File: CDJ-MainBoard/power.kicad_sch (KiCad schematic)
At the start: 46 parts, among them J15 USB_C_Receptacle_USB2.0_16P, SW3 SW_MAIN_POWER, U1 Compute_Module_5_Functional, U10 AP2112K-3.3 DIGITAL PSU LDO, U11 AP2112K-3.3 ANALOG AUDIO LDO, U12 CH224K, U13 SY8368AQQC

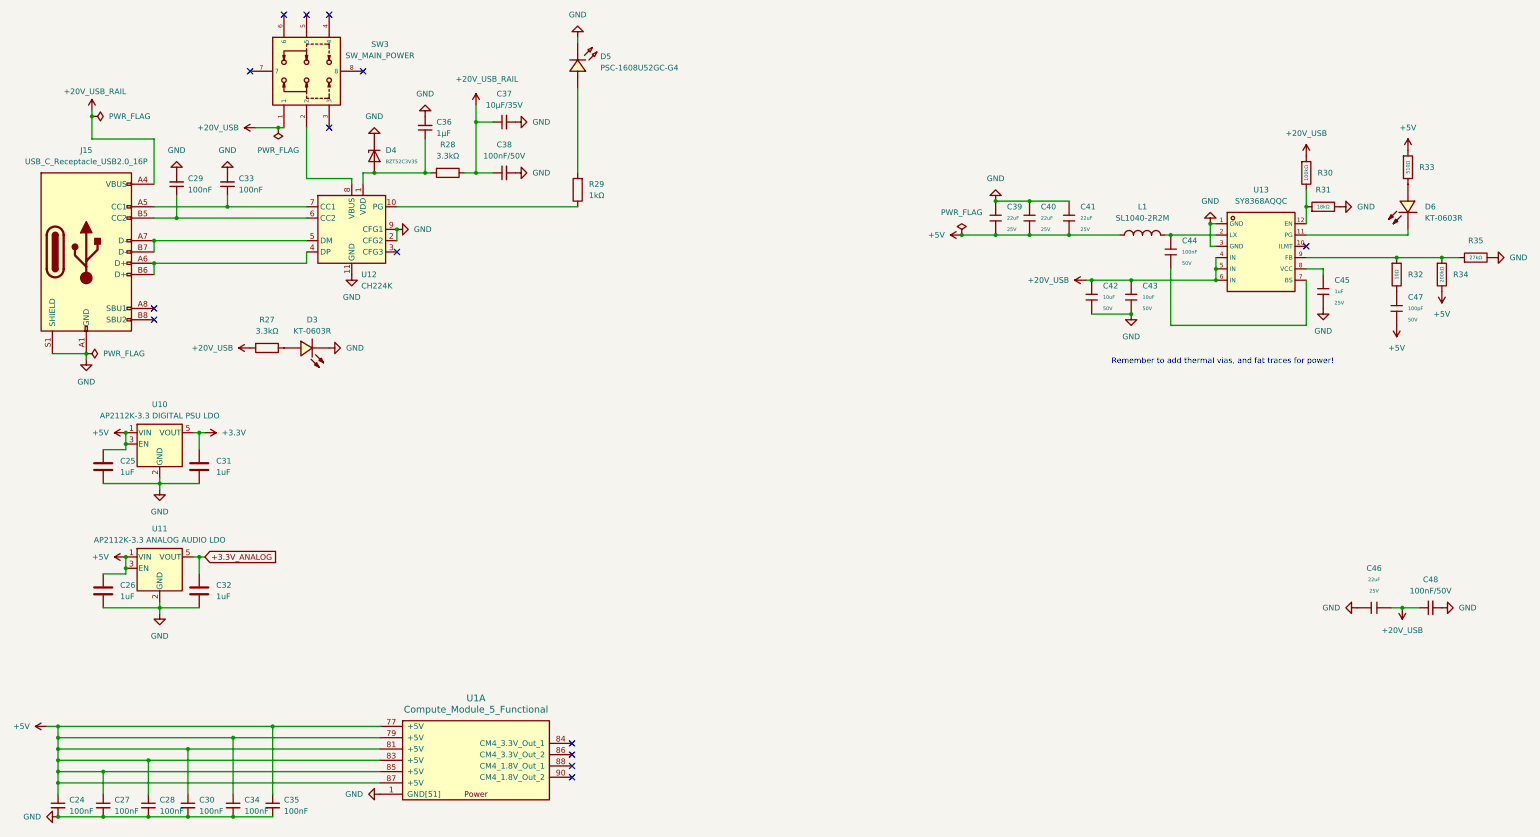
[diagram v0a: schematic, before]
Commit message: Route the buck and fixed pinout on ethernet and 3D model offsets
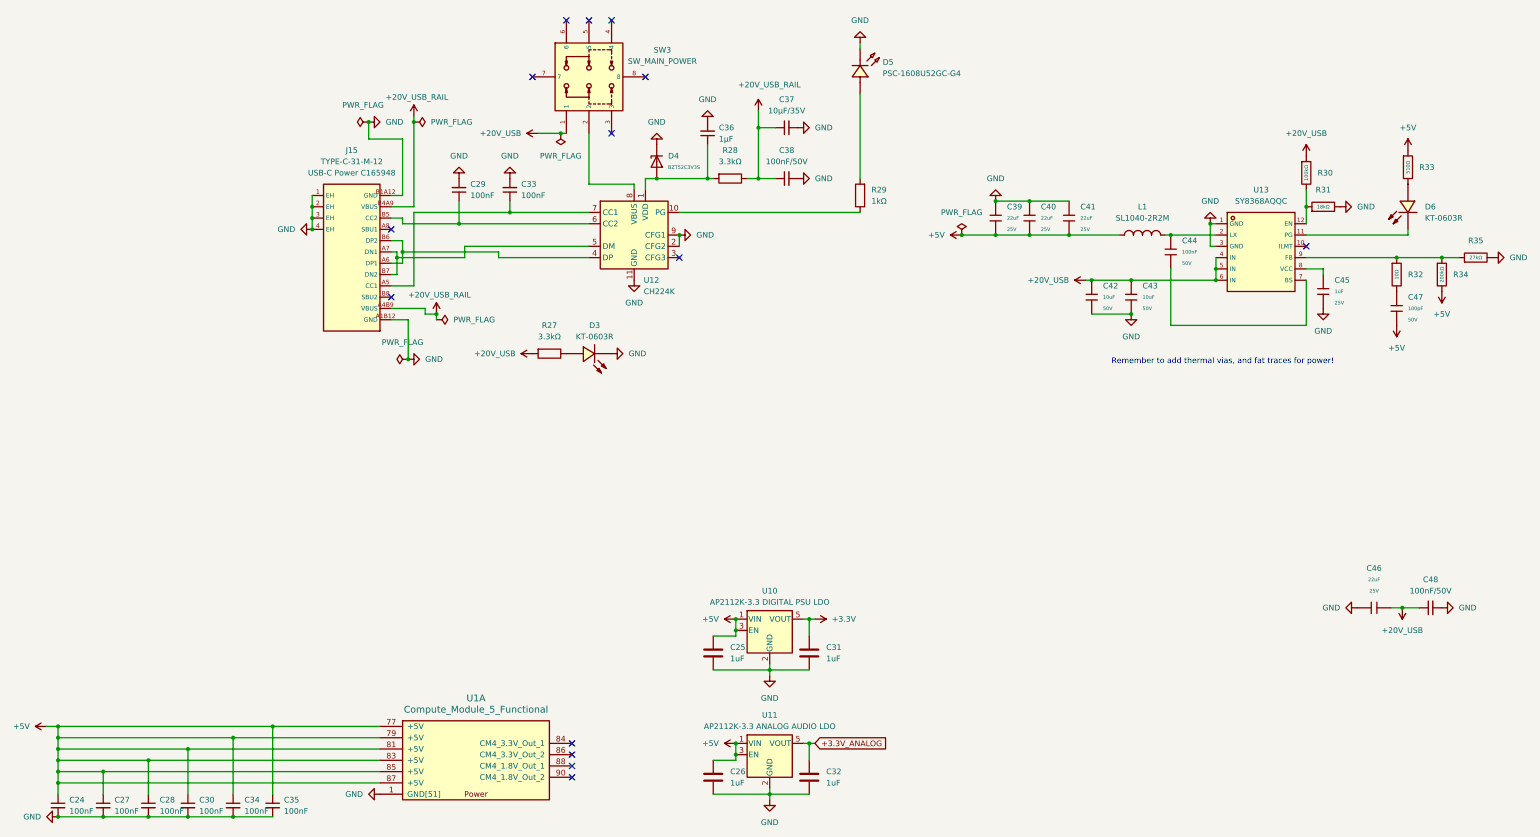
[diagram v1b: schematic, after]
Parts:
- removed J15: USB_C_Receptacle_USB2.0_16P, JLC2KiCad_lib-footprints:USB-C-SMD_TYPE-C-6PIN-2MD-073, symbol Connector:USB_C_Receptacle_USB2.0_16P
- added J15: TYPE-C-31-M-12, JLC2KiCad_lib-footprints:USB-C_SMD-TYPE-C-31-M-12_1, symbol TYPE-C-31-M-12:TYPE-C-31-M-12
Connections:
- net +20V_USB_RAIL: now also J15.A4B9 (VBUS), J15.B4A9 (VBUS)
- net GND: now also J15.1 (EH), J15.2 (EH), J15.3 (EH), J15.4 (EH), J15.A1B12 (GND), J15.B1A12 (GND)
- net at C29.1, U12.6 (CC2): now also J15.B5 (CC2)
- net at C33.1, U12.7 (CC1): now also J15.A5 (CC1)
- net at U12.4 (DP): now also J15.A6 (DP1), J15.B6 (DP2)
- net at U12.5 (DM): now also J15.A7 (DN1), J15.B7 (DN2)
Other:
- moved on the sheet: C25, C26, C29, C31, C32, C33, C36, C37, C38, D3, D4, D5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
